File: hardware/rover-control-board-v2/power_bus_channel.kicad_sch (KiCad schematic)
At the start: 33 parts, among them J15 TEMP_PROBE, Q15 Q_NMOS_DGS, Q16 Q_PMOS_DGS, Q17 Q_NMOS, Q18 CSD19533Q5A, U14 LTC7001, U15 ACS37003

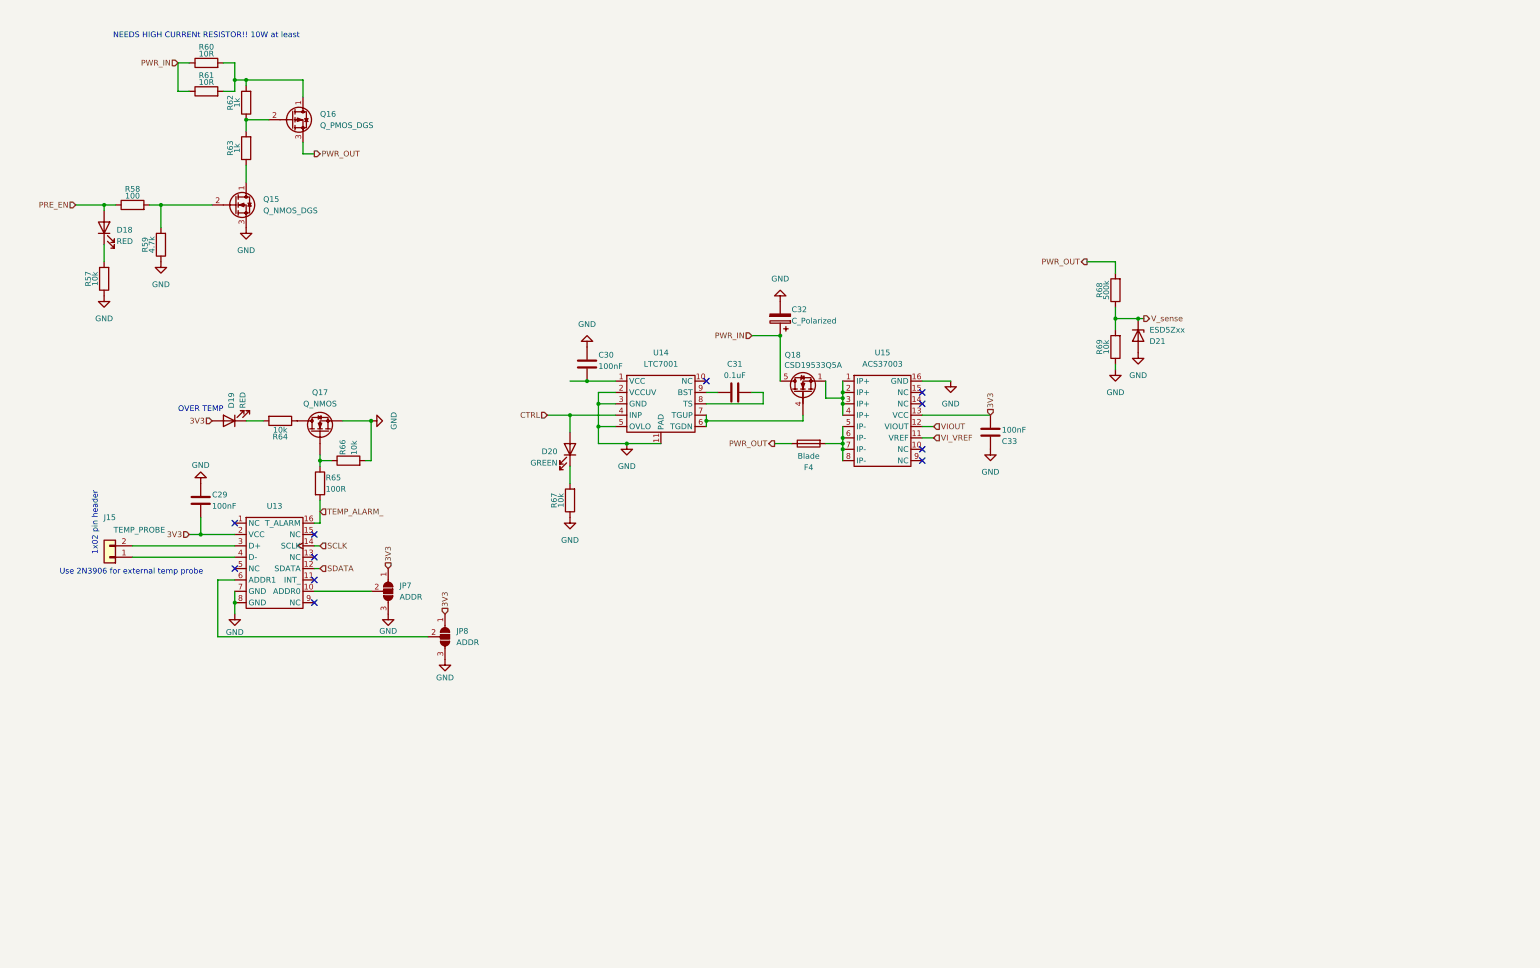
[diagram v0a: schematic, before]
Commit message: Added photovoltaic gate driver and ESD protection
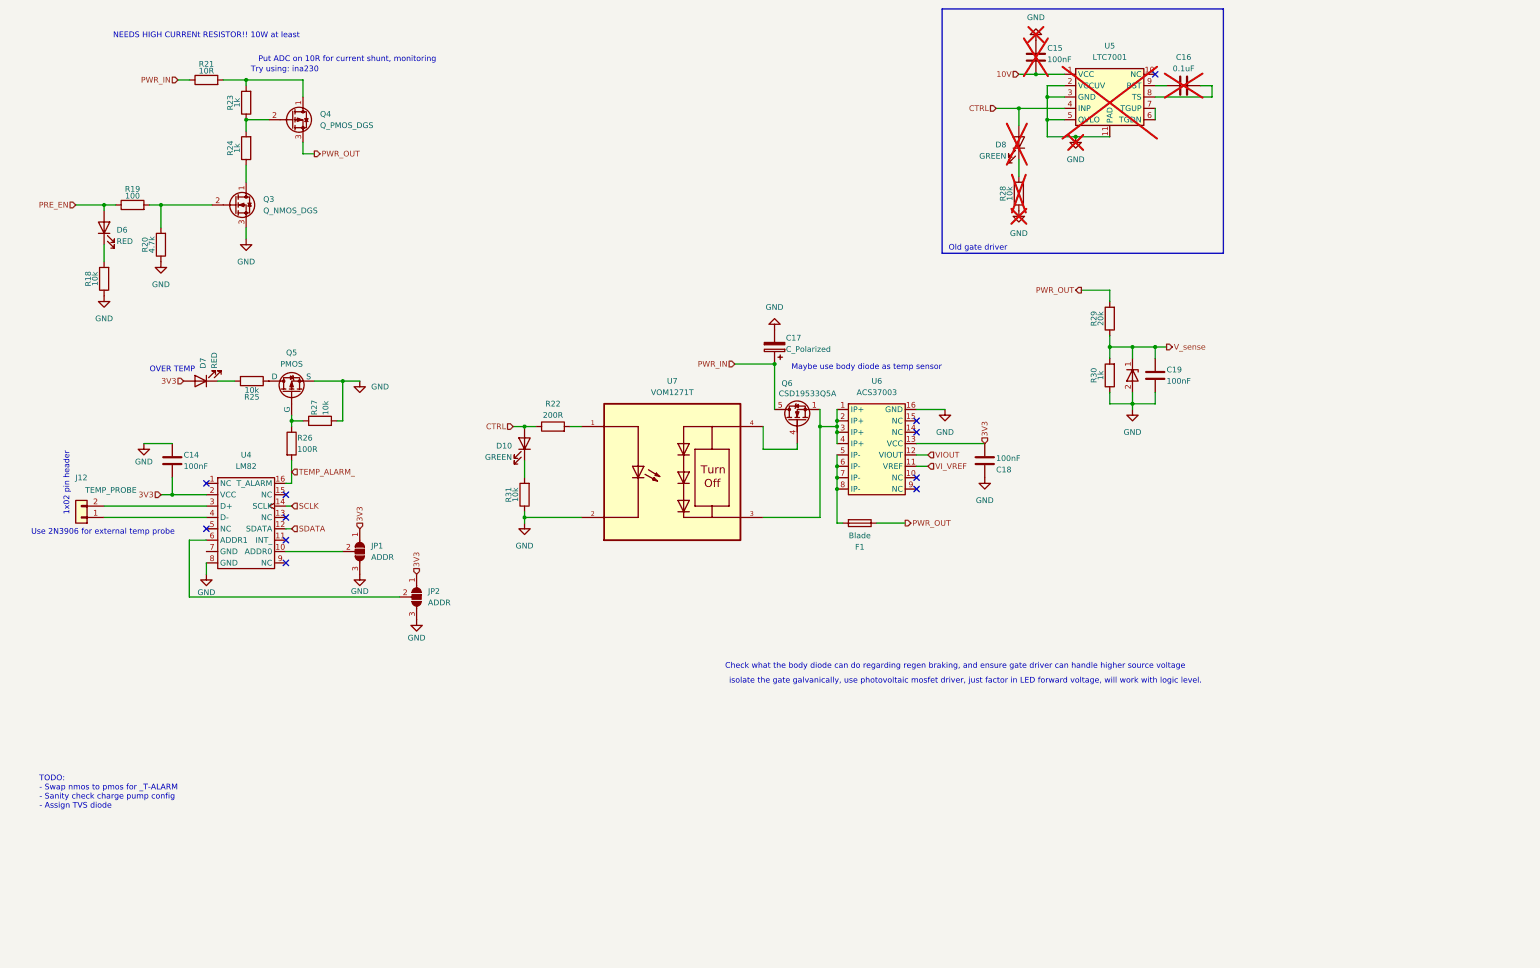
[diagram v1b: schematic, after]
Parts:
- removed C29, C30, C33: 100nF, symbol Device:C
- removed C31: 0.1uF, symbol Device:C
- removed C32: C_Polarized, Capacitor_SMD:CP_Elec_10x10.5, symbol Device:C_Polarized
- removed D18, D19: RED, symbol Device:LED
- removed D20: GREEN, symbol Device:LED
- removed D21: ESD5Zxx, Diode_SMD:D_SOD-523, symbol Diode:ESD5Zxx
- removed F4: Blade, symbol Device:Fuse
- removed J15: TEMP_PROBE, symbol Connector_Generic:Conn_01x02
- removed JP7, JP8: ADDR, Jumper:SolderJumper-3_P1.3mm_Open_Pad1.0x1.5mm, symbol Jumper:SolderJumper_3_Open
- removed Q15: Q_NMOS_DGS, symbol Transistor_FET:Q_NMOS_DGS
- removed Q16: Q_PMOS_DGS, symbol Transistor_FET:Q_PMOS_DGS
- removed Q17: Q_NMOS, symbol Device:Q_NMOS
- removed Q18: CSD19533Q5A, Package_TO_SOT_SMD:TDSON-8-1, symbol Transistor_FET:CSD19533Q5A
- removed R57, R64, R66, R67, R69: 10k, symbol Device:R
- removed R58: 100, symbol Device:R
- removed R59: 4.7k, symbol Device:R
- removed R60, R61: 10R, symbol Device:R
- removed R62, R63: 1k, symbol Device:R
- removed R65: 100R, symbol Device:R
- removed R68: 500k, symbol Device:R
- removed U13: (no value), footprints:LM82, symbol component_library:LM82
- removed U14: LTC7001, Package_SO:MSOP-10-1EP_3x3mm_P0.5mm_EP1.68x1.88mm, symbol component_library:LTC7001
- removed U15: ACS37003, Package_SO:SOIC-16W_7.5x10.3mm_P1.27mm, symbol component_library:ACS37003
- added C14, C15, C18, C19: 100nF, symbol Device:C
- added C16: 0.1uF, symbol Device:C
- added C17: C_Polarized, Capacitor_SMD:CP_Elec_10x10.5, symbol Device:C_Polarized
- added D10, D8: GREEN, symbol Device:LED
- added D6, D7: RED, symbol Device:LED
- added F1: Blade, symbol Device:Fuse
- added J12: TEMP_PROBE, symbol Connector_Generic:Conn_01x02
- added JP1, JP2: ADDR, Jumper:SolderJumper-3_P1.3mm_Open_Pad1.0x1.5mm, symbol Jumper:SolderJumper_3_Open
- added Q3: Q_NMOS_DGS, symbol Transistor_FET:Q_NMOS_DGS
- added Q4: Q_PMOS_DGS, symbol Transistor_FET:Q_PMOS_DGS
- added Q5: PMOS, symbol Simulation_SPICE:PMOS
- added Q6: CSD19533Q5A, Package_TO_SOT_SMD:TDSON-8-1, symbol Transistor_FET:CSD19533Q5A
- added R18, R25, R27, R28, R31: 10k, symbol Device:R
- added R19: 100, symbol Device:R
- added R20: 4.7k, symbol Device:R
- added R21: 10R, footprints:RES_PWR263S-35-10R0F, symbol Device:R
- added R22: 200R, Resistor_SMD:R_0603_1608Metric, symbol Device:R
- added R23, R24, R30: 1k, symbol Device:R
- added R26: 100R, symbol Device:R
- added R29: 20k, symbol Device:R
- added U2: (no value), Diode_SMD:D_SOD-882, symbol component_library:PESD3V3V1BLYL
- added U4: LM82, footprints:LM82, symbol component_library:LM82
- added U5: LTC7001, Package_SO:MSOP-10-1EP_3x3mm_P0.5mm_EP1.68x1.88mm, symbol component_library:LTC7001
- added U6: ACS37003, Package_SO:SOIC-16W_7.5x10.3mm_P1.27mm, symbol component_library:ACS37003
- added U7: VOM1271T, VOM1271T:SOIC254P695X242-4N, symbol component_library:VOM1271T
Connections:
- net 3V3: now also C14.2, C18.2, D7.2 (A), JP1.1 (A), JP2.1 (A), U4.2 (VCC), U6.13 (VCC)
- net CTRL: now also D10.2 (A), D8.2 (A), R22.1, U5.4 (INP)
- net GND: now also C14.1, C15.1, C17.2, C18.1, C19.2, JP1.3 (B), JP2.3 (B), Q3.3 (S), Q5.3 (S), R18.1, R20.1, R27.2, R28.1, R30.1, R31.1, U2.2 (A), U4.8 (GND), U5.11 (PAD), U5.2 (VCCUV), U5.3 (GND), U5.5 (OVLO), U6.16 (GND), U7.2
- net PRE_EN: now also D6.2 (A), R19.1
- net PWR_IN: now also C17.1, Q6.5 (D), R21.1
- net PWR_OUT: now also F1.1, Q4.3 (S), R29.2
- net SCLK: now also U4.14 (SCLK)
- net SDATA: now also U4.12 (SDATA)
- net TEMP_ALARM_: now also R26.2, U4.16 (T_ALARM)
- net VIOUT: now also U6.12 (VIOUT)
- net VI_VREF: now also U6.11 (VREF)
- net V_sense: now also C19.1, R29.1, R30.2, U2.1 (K)
- new net: Q3.1 (D), R24.1
- new net: Q4.2 (G), R23.1, R24.2
- new net: D7.1 (K), R25.2
- new net: J12.1 (Pin_1), U4.4 (D-)
- new net: J12.2 (Pin_2), U4.3 (D+)
- new net: R22.2, U7.1
- new net: JP2.2 (C), U4.6 (ADDR1)
- new net: Q6.1 (S), Q6.2 (S), Q6.3 (S), U6.1 (IP+), U6.2 (IP+), U6.3 (IP+), U6.4 (IP+), U7.3
- new net: Q6.4 (G), U7.4
- new net: JP1.2 (C), U4.10 (ADDR0)
- new net: U5.6 (TGDN), U5.7 (TGUP)
- new net: C16.2, U5.8 (TS)
- new net: C16.1, U5.9 (BST)
- new net: Q3.2 (G), R19.2, R20.2
- new net: D6.1 (K), R18.2
- new net: F1.2, U6.5 (IP-), U6.6 (IP-), U6.7 (IP-), U6.8 (IP-)
- new net: Q5.1 (D), R25.1
- new net: Q4.1 (D), R21.2, R23.2
- new net: D10.1 (K), R31.2
- new net: D8.1 (K), R28.2
- new net: Q5.2 (G), R26.1, R27.1
- new net 10V: C15.2, U5.1 (VCC)
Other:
- note added: "Check what the body diode can do regarding regen braking, and ensure gate driver can handle higher source voltage"
- note added: "Maybe use body diode as temp sensor"
- note added: "Old gate driver"
- note added: "Put ADC on 10R for current shunt, monitoring"
- note added: "TODO: - Swap nmos to pmos for _T-ALARM - Sanity check charge pump config - Assign TVS diode"
- note added: "Try using: ina230"
- note added: "isolate the gate galvanically, use photovoltaic mosfet driver, just factor in LED forward voltage, will work with logic level."

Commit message: footprints and BOM additions
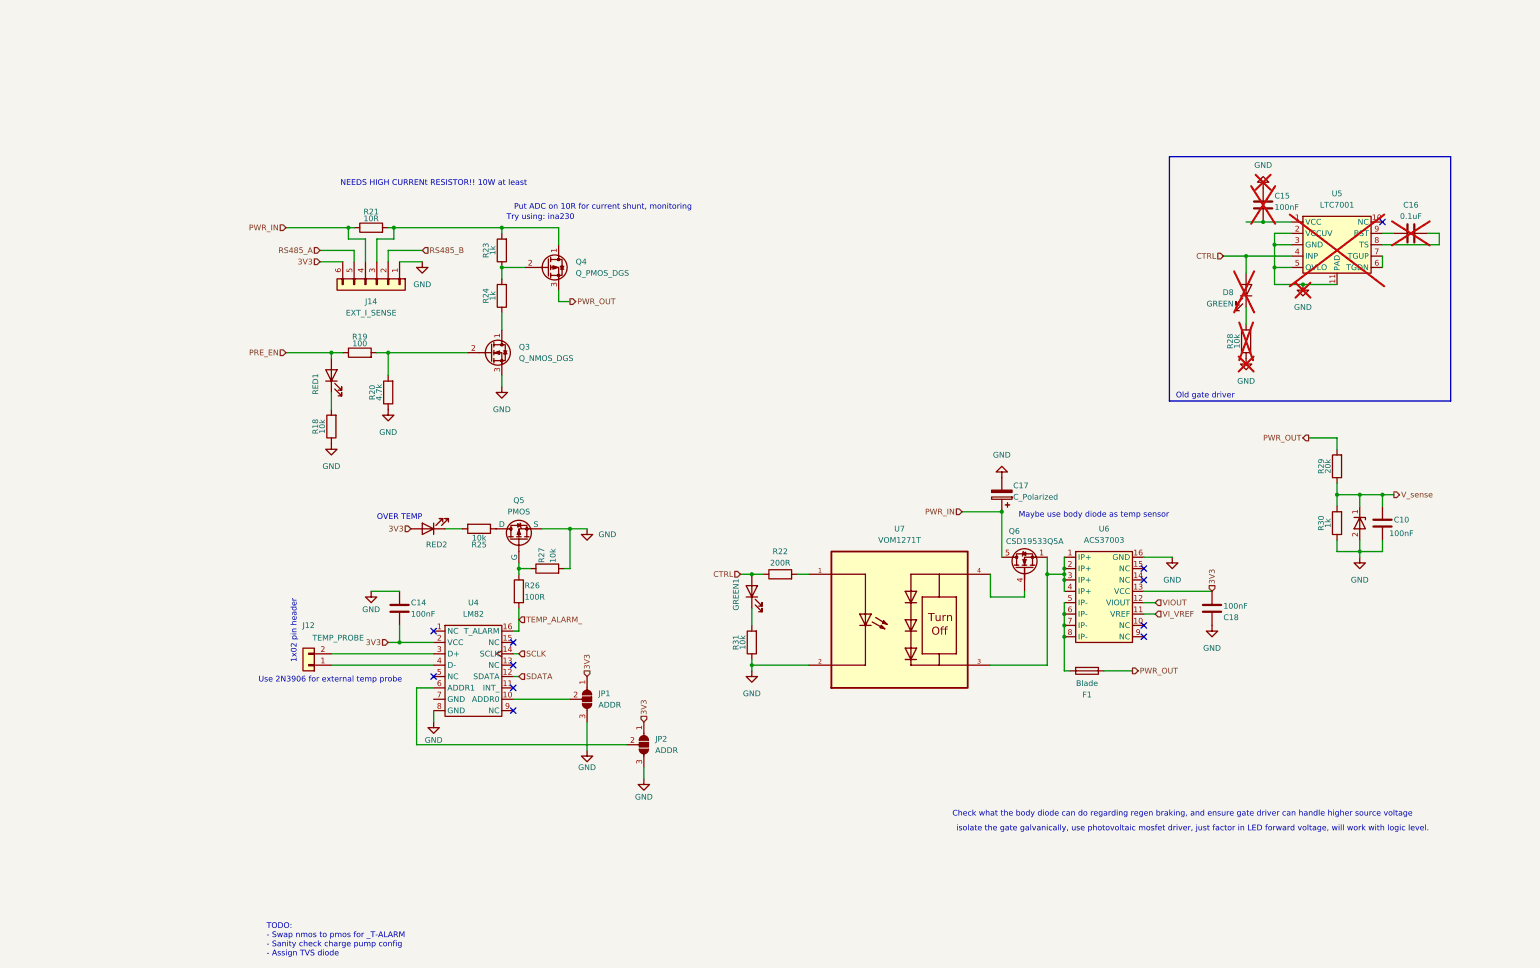
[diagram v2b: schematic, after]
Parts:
- removed C19: 100nF, symbol Device:C
- removed D10: GREEN, symbol Device:LED
- removed D6, D7: RED, symbol Device:LED
- added C10: 100nF, Capacitor_SMD:C_0603_1608Metric, symbol Device:C
- added GREEN1: 350-599, LED_SMD:LED_0805_2012Metric, symbol Device:LED
- added J14: EXT_I_SENSE, Connector_PinHeader_2.54mm:PinHeader_1x06_P2.54mm_Vertical, symbol Connector_Generic:Conn_01x06
- added RED1, RED2: 5991110147F, LED_SMD:LED_0805_2012Metric, symbol Device:LED
- C14, C18: footprint (none) -> Capacitor_SMD:C_0603_1608Metric
- F1: footprint (none) -> Fuse:Fuseholder_Keystone_3555-2
- J12: footprint (none) -> Connector_JST:JST_XH_B2B-XH-A_1x02_P2.50mm_Vertical
- R18, R19, R20, R23, R24, R25, R26, R27, R29, R30, R31: footprint (none) -> Resistor_SMD:R_0603_1608Metric
- U7: footprint VOM1271T:SOIC254P695X242-4N -> footprints:SOIC254P695X242-4N
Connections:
- net 3V3: now also J14.6 (Pin_6), RED2.2 (A)
- net CTRL: now also GREEN1.2 (A)
- net GND: now also C10.2, J14.1 (Pin_1)
- net PRE_EN: now also RED1.2 (A)
- net PWR_IN: now also J14.4 (Pin_4)
- net V_sense: now also C10.1
- net at R25.2: now also RED2.1 (K)
- net at R18.2: now also RED1.1 (K)
- net at Q4.1 (D), R21.2, R23.2: now also J14.3 (Pin_3)
- net at R31.2: now also GREEN1.1 (K)
- net 10V: no longer names the net of C15.2, U5.1 (VCC)
- new net RS485_A: J14.5 (Pin_5)
- new net RS485_B: J14.2 (Pin_2)
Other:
- title: (none) -> Rover Control Board
- moved on the sheet: C14, C15, C16, C17, C18, D8, F1, J12, JP1, JP2, Q3, Q4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

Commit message: BOM
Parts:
- removed Q3: Q_NMOS_DGS, symbol Transistor_FET:Q_NMOS_DGS
- removed Q4: Q_PMOS_DGS, symbol Transistor_FET:Q_PMOS_DGS
- added Q1: NMOS_GDS, Package_TO_SOT_SMD:SOT-223, symbol Transistor_FET_Other:Q_NMOS_Depletion_GDS
- added Q4: Q_PMOS_GDS, Package_TO_SOT_SMD:TO-252-2, symbol Transistor_FET:Q_PMOS_GDS
- C10, C14, C18: digikey_part_num (none) -> 311-1344-1-ND
- C15: footprint (none) -> Capacitor_SMD:C_0603_1608Metric; digikey_part_num (none) -> 311-1344-1-ND
- C16: value 0.1uF -> 100nF; footprint (none) -> Capacitor_SMD:C_0603_1608Metric; digikey_part_num (none) -> 311-1344-1-ND
- F1: digikey_part_num (none) -> 36-3555-2-ND
- GREEN1: digikey_part_num (none) -> 350-5991180147FCT-ND
- J12: digikey_part_num (none) -> 455-B2B-XH-A-ND
- J14: now not fitted
- Q5: footprint (none) -> Package_TO_SOT_SMD:SOT-323_SC-70; digikey_part_num (none) -> 1727-1229-1-ND
- Q6: digikey_part_num (none) -> 296-37479-1-ND
- R18, R25, R27, R31: digikey_part_num (none) -> 311-10.0KHRCT-ND
- R19: value 100 -> 100R; digikey_part_num (none) -> 541-100HCT-ND
- R20: digikey_part_num (none) -> 311-4.70KHRCT-ND
- R22: digikey_part_num (none) -> 311-200GRCT-ND
- R23, R24, R30: digikey_part_num (none) -> YAG1237CT-ND
- R26: digikey_part_num (none) -> 541-100HCT-ND
- R29: digikey_part_num (none) -> 2019-RN73R1JTTD2002B25CT-ND
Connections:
- net GND: now also Q1.3 (S)
- net PWR_OUT: now also Q4.3 (S)
- net at R24.1: now also Q1.2 (D)
- net at R23.1, R24.2: now also Q4.1 (G)
- net at R19.2, R20.2: now also Q1.1 (G)
- net at J14.3 (Pin_3), R21.2, R23.2: now also Q4.2 (D)

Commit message: Finished BOM
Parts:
- RED1, RED2: digikey_part_num (none) -> 350-5991110147FCT-ND
- U2: value (none) -> D3V3M1U2S9-7; digikey_part_num (none) -> 31-D3V3M1U2S9-7CT-ND
- U4: digikey_part_num (none) -> 296-35317-1-ND
- U6: digikey_part_num (none) -> 620-ACS37003KMCATR-180B5CT-ND
- U7: footprint footprints:SOIC254P695X242-4N -> Package_SO:SOP-4_3.8x4.1mm_P2.54mm; digikey_part_num (none) -> VOM1271TCT-ND
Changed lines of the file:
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@@
 			)
 		)
-		(property "Footprint" "footprints:SOIC254P695X242-4N"
+		(property "Footprint" "Package_SO:SOP-4_3.8x4.1mm_P2.54mm"
 			(at 209.55 149.86 0)
 			(hide yes)
@@
 				)
 				(justify bottom)
+			)
+		)
+		(property "digikey_part_num" "VOM1271TCT-ND"
+			(at 209.55 149.86 0)
+			(hide yes)
+			(show_name no)
+			(do_not_autoplace no)
+			(effects
+				(font
+					(size 1.27 1.27)
+				)
 			)
 		)
@@
 			)
 		)
-		(property "Value" ""
+		(property "Value" "D3V3M1U2S9-7"
 			(at 312.42 128.27 0)
 			(show_name no)
@@
 		)
 		(property "Description" ""
+			(at 312.42 128.27 0)
+			(hide yes)
+			(show_name no)
+			(do_not_autoplace no)
+			(effects
+				(font
+					(size 1.27 1.27)
+				)
+			)
+		)
+		(property "digikey_part_num" "31-D3V3M1U2S9-7CT-ND"
 			(at 312.42 128.27 0)
 			(hide yes)
@@
 			)
 		)
+		(property "digikey_part_num" "620-ACS37003KMCATR-180B5CT-ND"
+			(at 255.27 144.78 0)
+			(hide yes)
+			(show_name no)
+			(do_not_autoplace no)
+			(effects
+				(font
+					(size 1.27 1.27)
+				)
+			)
+		)
 		(pin "8"
 		)
@@
 			)
 		)
+		(property "digikey_part_num" "350-5991110147FCT-ND"
+			(at 104.14 129.54 0)
+			(hide yes)
+			(show_name no)
+			(do_not_autoplace no)
+			(effects
+				(font
+					(size 1.27 1.27)
+				)
+			)
+		)
 		(pin "1"
 		)
@@
 			)
 		)
+		(property "digikey_part_num" "350-5991110147FCT-ND"
+			(at 82.55 95.25 0)
+			(hide yes)
+			(show_name no)
+			(do_not_autoplace no)
+			(effects
+				(font
+					(size 1.27 1.27)
+				)
+			)
+		)
 		(pin "1"
 		)
@@
 			(at 114.3 157.48 0)
 			(hide yes)
+			(show_name no)
+			(do_not_autoplace no)
+			(effects
+				(font
+					(size 1.27 1.27)
+				)
+			)
+		)
+		(property "digikey_part_num" "296-35317-1-ND"
+			(at 114.3 157.48 0)
+			(hide yes)

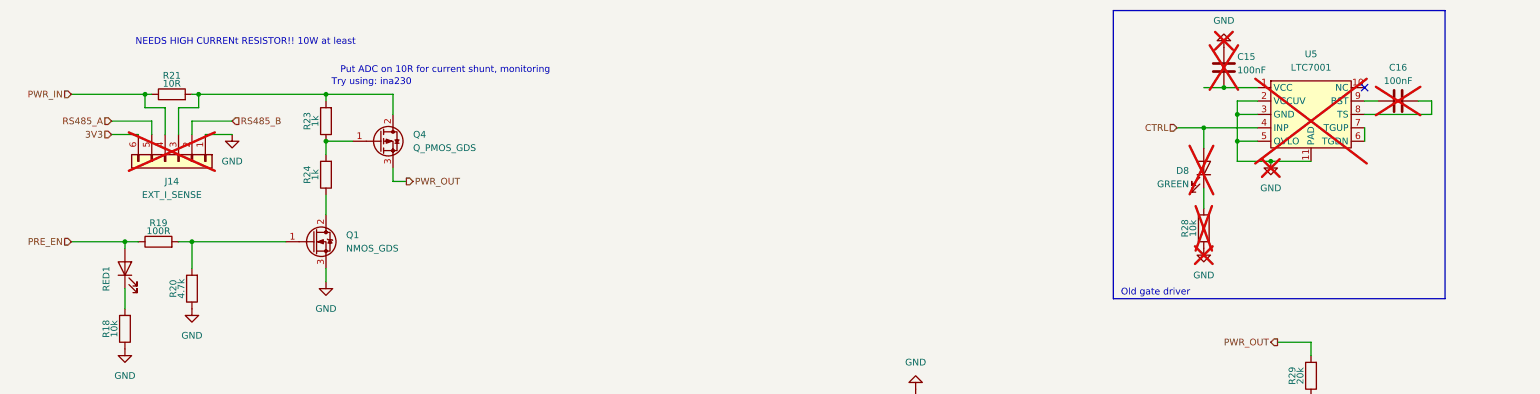
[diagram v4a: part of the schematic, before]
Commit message: Initial component placement, finalising schematic
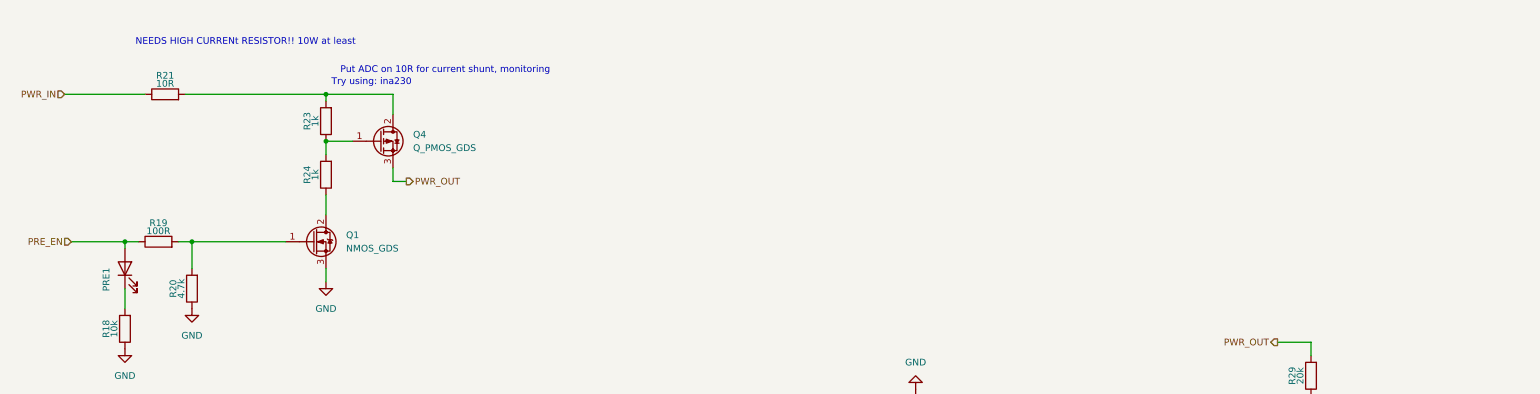
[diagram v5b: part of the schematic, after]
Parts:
- removed C15, C16: 100nF, Capacitor_SMD:C_0603_1608Metric, symbol Device:C
- removed D8: GREEN, symbol Device:LED
- removed J14: EXT_I_SENSE, Connector_PinHeader_2.54mm:PinHeader_1x06_P2.54mm_Vertical, symbol Connector_Generic:Conn_01x06
- removed R28: 10k, symbol Device:R
- removed U5: LTC7001, Package_SO:MSOP-10-1EP_3x3mm_P0.5mm_EP1.68x1.88mm, symbol component_library:LTC7001
- renumbered RED1 to PRE1
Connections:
- no-connect marks 11 -> 10
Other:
- note removed: "Old gate driver"
- moved on the sheet: R21
